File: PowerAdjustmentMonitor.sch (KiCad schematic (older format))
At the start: 19 parts

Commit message: Refactoring and Created key shortcuts
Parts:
- removed R? (x2): R, ~, symbol R
- removed U? (x2): LM324, symbol LM324
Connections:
- net labels removed: V+_CURR_MON, V+_MON, V-_CURR_MON, V-_MON
- wire segments 75 -> 53
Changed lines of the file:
@@
 $Descr A4 11693 8268
 encoding utf-8
-Sheet 9 9
+Sheet 7 9
 Title ""
-Date "9 feb 2014"
+Date "18 feb 2014"
 Rev ""
 Comp ""
@@
 Wire Wire Line
 	3150 1650 3150 1500
-Connection ~ 3150 800
 Connection ~ 3150 1650
 $Comp
@@
 Wire Wire Line
 	4050 1650 4050 1750
-Text HLabel 5700 800  0    60   Output ~ 0
+Text HLabel 5700 800  2    60   Output ~ 0
 V+_ADJ
-Text HLabel 5500 5700 0    60   Output ~ 0
+Text HLabel 5500 5700 2    60   Output ~ 0
 V-_ADJ
-Text HLabel 10100 2300 0    60   Output ~ 0
+Text HLabel 10100 2300 2    60   Output ~ 0
 3V3_MON
-Text HLabel 10100 2550 0    60   Output ~ 0
+Text HLabel 10100 2550 2    60   Output ~ 0
 5V_MON
-Text HLabel 10100 2900 0    60   Output ~ 0
+Text HLabel 10100 2900 2    60   Output ~ 0
 V+_ADJ_MON
-Text HLabel 10100 3200 0    60   Output ~ 0
+Text HLabel 10100 3200 2    60   Output ~ 0
 V-_ADJ_MON
-Text HLabel 10200 4550 0    60   Output ~ 0
-V+_CURR_MON
-Text HLabel 10200 6000 0    60   Output ~ 0
-V-_CURR_MON
 $Comp
 L R R?
@@
 Wire Wire Line
 	8850 2300 10100 2300
-$Comp
-L R R?
-U 1 1 52F6ED35
-P 4050 5700
-F 0 "R?" V 4130 5700 40  0000 C CNN
-F 1 "R" V 4057 5701 40  0000 C CNN
-F 2 "~" V 3980 5700 30  0000 C CNN
-F 3 "~" H 4050 5700 30  0000 C CNN
-	1    4050 5700
-	0    -1   -1   0
-$EndComp
-Wire Wire Line
-	2900 5700 3800 5700
-Wire Wire Line
-	4300 5700 5500 5700
-Wire Wire Line
-	2850 800  3700 800
-Wire Wire Line
-	4200 800  5700 800
-$Comp
-L R R?
-U 1 1 52F6EEF0
-P 3950 800
-F 0 "R?" V 4030 800 40  0000 C CNN
-F 1 "R" V 3957 801 40  0000 C CNN
-F 2 "~" V 3880 800 30  0000 C CNN
-F 3 "~" H 3950 800 30  0000 C CNN
-	1    3950 800
-	0    -1   -1   0
-$EndComp
-Wire Wire Line
-	3600 5700 3600 5500
-Wire Wire Line
-	3600 5500 4150 5500
-Connection ~ 3600 5700
-Text Label 3850 5500 0    60   ~ 0
-V-_MON
-Wire Wire Line
-	3550 800  3550 1150
-Wire Wire Line
-	3550 1150 4250 1150
-Connection ~ 3550 800
-Text Label 3850 1150 0    60   ~ 0
-V+_MON
-$Comp
-L LM324 U?
-U 1 1 52F6FECD
-P 8800 6000
-F 0 "U?" H 8850 6200 60  0000 C CNN
-F 1 "LM324" H 8950 5800 50  0000 C CNN
-F 2 "" H 8800 6000 60  0000 C CNN
-F 3 "" H 8800 6000 60  0000 C CNN
-	1    8800 6000
-	1    0    0    -1
-$EndComp
-$Comp
-L +12V #PWR?
-U 1 1 52F6FEE1
-P 8700 5500
-F 0 "#PWR?" H 8700 5450 20  0001 C CNN
-F 1 "+12V" H 8700 5600 30  0000 C CNN
-F 2 "" H 8700 5500 60  0000 C CNN
-F 3 "" H 8700 5500 60  0000 C CNN
-	1    8700 5500
-	-1   0    0    -1
-$EndComp
-$Comp
-L -12V #PWR?
-U 1 1 52F6FEF0
-P 8700 6600
-F 0 "#PWR?" H 8700 6730 20  0001 C CNN
-F 1 "-12V" H 8700 6700 30  0000 C CNN
-F 2 "" H 8700 6600 60  0000 C CNN
-F 3 "" H 8700 6600 60  0000 C CNN
-	1    8700 6600
-	1    0    0    1
-$EndComp
-Wire Wire Line
-	8700 5500 8700 5600
-Wire Wire Line
-	8700 6400 8700 6600
-$Comp
-L LM324 U?
-U 1 1 52F6FFA1
-P 8800 4550
-F 0 "U?" H 8850 4750 60  0000 C CNN
-F 1 "LM324" H 8950 4350 50  0000 C CNN
-F 2 "" H 8800 4550 60  0000 C CNN
-F 3 "" H 8800 4550 60  0000 C CNN
-	1    8800 4550
-	1    0    0    -1
-$EndComp
-$Comp
-L +12V #PWR?
-U 1 1 52F6FFA7
-P 8700 4050
-F 0 "#PWR?" H 8700 4000 20  0001 C CNN
-F 1 "+12V" H 8700 4150 30  0000 C CNN
-F 2 "" H 8700 4050 60  0000 C CNN
-F 3 "" H 8700 4050 60  0000 C CNN
-	1    8700 4050
-	-1   0    0    -1
-$EndComp
-$Comp
-L -12V #PWR?
-U 1 1 52F6FFAD
-P 8700 5150
-F 0 "#PWR?" H 8700 5280 20  0001 C CNN
-F 1 "-12V" H 8700 5250 30  0000 C CNN
-F 2 "" H 8700 5150 60  0000 C CNN
-F 3 "" H 8700 5150 60  0000 C CNN
-	1    8700 5150
-	1    0    0    1
-$EndComp
-Wire Wire Line
-	8700 4050 8700 4150
-Wire Wire Line
-	8700 4950 8700 5150
-Wire Wire Line
-	9300 4550 10200 4550
-Wire Wire Line
-	9300 6000 10200 6000
-Wire Wire Line
-	8300 4650 8200 4650
-Wire Wire Line
-	8200 4650 8200 5300
-Wire Wire Line
-	8200 5300 9450 5300
-Wire Wire Line
-	9450 5300 9450 4550
-Connection ~ 9450 4550
-Wire Wire Line
-	8300 6100 8150 6100
-Wire Wire Line
-	8150 6100 8150 6800
-Wire Wire Line
-	8150 6800 9450 6800
-Wire Wire Line
-	9450 6800 9450 6000
-Connection ~ 9450 6000
-Wire Wire Line
-	8300 5900 7550 5900
-Wire Wire Line
-	8300 4450 7600 4450
-Text Label 7700 4450 0    60   ~ 0
-V+_MON
-Text Label 7650 5900 0    60   ~ 0
-V-_MON
+Wire Wire Line
+	2900 5700 5500 5700
+Wire Wire Line
+	2850 800  5700 800
 $Comp
 L RVAR R?

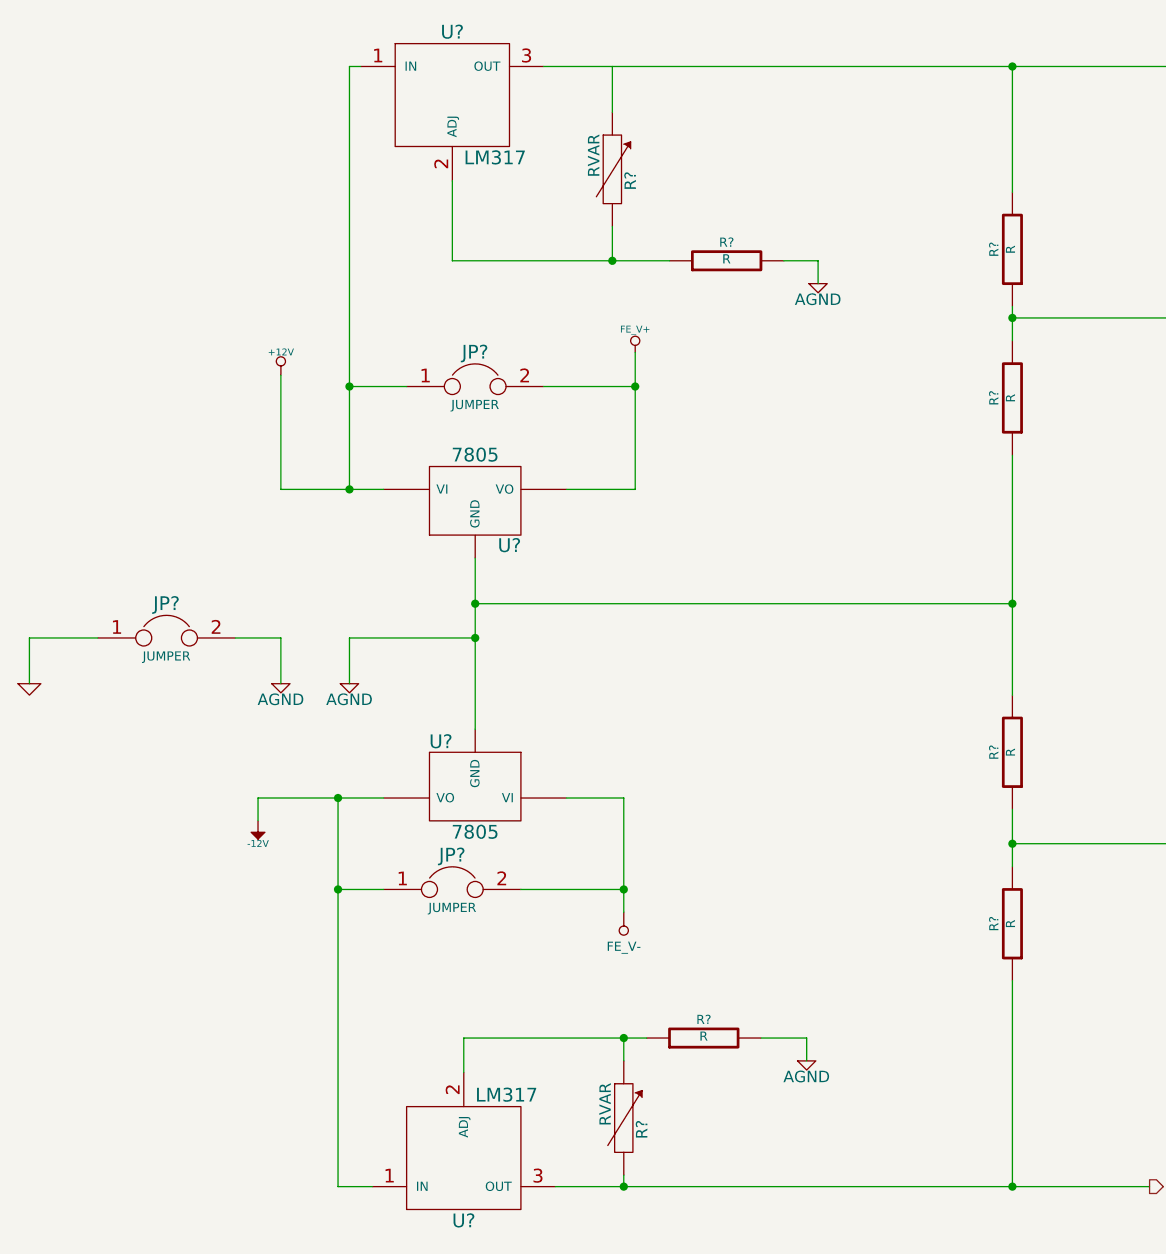
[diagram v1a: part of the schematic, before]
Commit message: Relay module association and placement
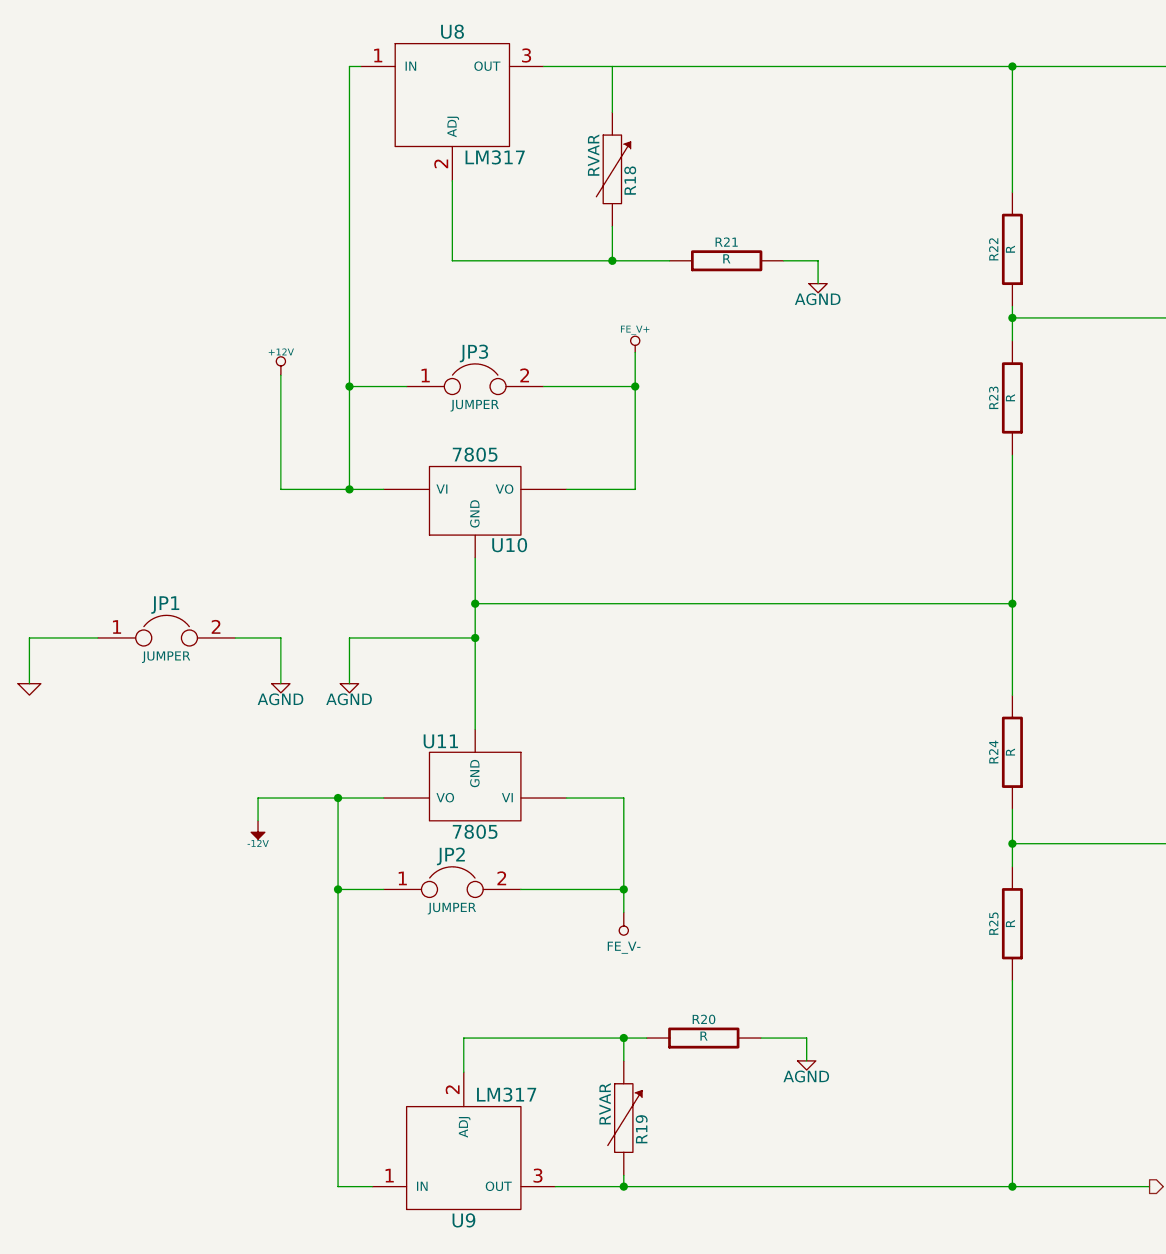
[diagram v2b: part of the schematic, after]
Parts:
- gave numbers to parts that had none: 15
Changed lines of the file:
@@
 Sheet 7 9
 Title ""
-Date "18 feb 2014"
+Date "20 feb 2014"
 Rev ""
 Comp ""
@@
 $EndDescr
 $Comp
-L +5V #PWR?
+L +5V #PWR034
 U 1 1 52F69910
 P 8550 2050
-F 0 "#PWR?" H 8550 2140 20  0001 C CNN
+F 0 "#PWR034" H 8550 2140 20  0001 C CNN
 F 1 "+5V" H 8550 2140 30  0000 C CNN
 F 2 "" H 8550 2050 60  0000 C CNN
@@
 $EndComp
 $Comp
-L +3.3V #PWR?
+L +3.3V #PWR035
 U 1 1 52F69916
 P 8850 2050
-F 0 "#PWR?" H 8850 2010 30  0001 C CNN
+F 0 "#PWR035" H 8850 2010 30  0001 C CNN
 F 1 "+3.3V" H 8850 2160 30  0000 C CNN
 F 2 "" H 8850 2050 60  0000 C CNN
@@
 $EndComp
 $Comp
-L -12V #PWR?
+L -12V #PWR036
 U 1 1 52F699A1
 P 1600 4100
-F 0 "#PWR?" H 1600 4230 20  0001 C CNN
+F 0 "#PWR036" H 1600 4230 20  0001 C CNN
 F 1 "-12V" H 1600 4200 30  0000 C CNN
 F 2 "" H 1600 4100 60  0000 C CNN
@@
 $EndComp
 $Comp
-L +12V #PWR?
+L +12V #PWR037
 U 1 1 52F699A7
 P 1700 2150
-F 0 "#PWR?" H 1700 2100 20  0001 C CNN
+F 0 "#PWR037" H 1700 2100 20  0001 C CNN
 F 1 "+12V" H 1700 2250 30  0000 C CNN
 F 2 "" H 1700 2150 60  0000 C CNN
@@
 	1700 2150 1700 2650
 $Comp
-L LM317 U?
+L LM317 U8
 U 1 1 52F69E71
 P 2450 950
-F 0 "U?" H 2450 1250 60  0000 C CNN
+F 0 "U8" H 2450 1250 60  0000 C CNN
 F 1 "LM317" H 2500 700 60  0000 L CNN
 F 2 "~" H 2450 950 60  0000 C CNN
@@
 $EndComp
 $Comp
-L LM317 U?
+L LM317 U9
 U 1 1 52F69E80
 P 2500 5550
-F 0 "U?" H 2500 5850 60  0000 C CNN
+F 0 "U9" H 2500 5850 60  0000 C CNN
 F 1 "LM317" H 2550 5300 60  0000 L CNN
 F 2 "~" H 2500 5550 60  0000 C CNN
@@
 	1600 4000 2150 4000
 $Comp
-L JUMPER JP?
+L JUMPER JP2
 U 1 1 52F69EAE
 P 2450 4400
-F 0 "JP?" H 2450 4550 60  0000 C CNN
+F 0 "JP2" H 2450 4550 60  0000 C CNN
 F 1 "JUMPER" H 2450 4320 40  0000 C CNN
 F 2 "~" H 2450 4400 60  0000 C CNN
@@
 	3200 4000 2950 4000
 $Comp
-L JUMPER JP?
+L JUMPER JP3
 U 1 1 52F69ECB
 P 2550 2200
-F 0 "JP?" H 2550 2350 60  0000 C CNN
+F 0 "JP3" H 2550 2350 60  0000 C CNN
 F 1 "JUMPER" H 2550 2120 40  0000 C CNN
 F 2 "~" H 2550 2200 60  0000 C CNN
@@
 	3250 2200 2850 2200
 $Comp
-L GND #PWR?
+L GND #PWR038
 U 1 1 52F69EEF
 P 600 3500
-F 0 "#PWR?" H 600 3500 30  0001 C CNN
+F 0 "#PWR038" H 600 3500 30  0001 C CNN
 F 1 "GND" H 600 3430 30  0001 C CNN
 F 2 "" H 600 3500 60  0000 C CNN
@@
 $EndComp
 $Comp
-L AGND #PWR?
+L AGND #PWR039
 U 1 1 52F69F10
 P 1700 3500
-F 0 "#PWR?" H 1700 3500 40  0001 C CNN
+F 0 "#PWR039" H 1700 3500 40  0001 C CNN
 F 1 "AGND" H 1700 3430 50  0000 C CNN
 F 2 "" H 1700 3500 60  0000 C CNN
@@
 $EndComp
 $Comp
-L JUMPER JP?
+L JUMPER JP1
 U 1 1 52F69F27
 P 1200 3300
-F 0 "JP?" H 1200 3450 60  0000 C CNN
+F 0 "JP1" H 1200 3450 60  0000 C CNN
 F 1 "JUMPER" H 1200 3220 40  0000 C CNN
 F 2 "~" H 1200 3300 60  0000 C CNN
@@
 	1700 3300 1700 3500
 $Comp
-L AGND #PWR?
+L AGND #PWR040
 U 1 1 52F69F75
 P 2000 3500
-F 0 "#PWR?" H 2000 3500 40  0001 C CNN
+F 0 "#PWR040" H 2000 3500 40  0001 C CNN
 F 1 "AGND" H 2000 3430 50  0000 C CNN
 F 2 "" H 2000 3500 60  0000 C CNN
@@
 	2000 3500 2000 3300
 $Comp
-L FE_V+ #PWR?
+L FE_V+ #PWR041
 U 1 1 52F6E408
 P 3250 2050
-F 0 "#PWR?" H 3250 2150 30  0001 C CNN
+F 0 "#PWR041" H 3250 2150 30  0001 C CNN
 F 1 "FE_V+" H 3250 2150 30  0000 C CNN
 F 2 "" H 3250 2050 60  0000 C CNN
@@
 Connection ~ 3250 2200
 $Comp
-L FE_V- #PWR?
+L FE_V- #PWR41
 U 1 1 52F6E430
 P 3200 4500
-F 0 "#PWR?" H 3200 4700 40  0001 C CNN
+F 0 "#PWR41" H 3200 4700 40  0001 C CNN
 F 1 "FE_V-" H 3200 4650 40  0000 C CNN
 F 2 "" H 3200 4500 60  0000 C CNN
@@
 Connection ~ 3200 4400
 $Comp
-L 7805 U?
+L 7805 U10
 U 1 1 52F6E65F
 P 2550 2700
-F 0 "U?" H 2700 2504 60  0000 C CNN
+F 0 "U10" H 2700 2504 60  0000 C CNN
 F 1 "7805" H 2550 2900 60  0000 C CNN
 F 2 "~" H 2550 2700 60  0000 C CNN
@@
 $EndComp
 $Comp
-L 7805 U?
+L 7805 U11
 U 1 1 52F6E66C
 P 2550 3950
-F 0 "U?" H 2700 3754 60  0000 C CNN
+F 0 "U11" H 2700 3754 60  0000 C CNN
 F 1 "7805" H 2550 4150 60  0000 C CNN
 F 2 "~" H 2550 3950 60  0000 C CNN
@@
 Connection ~ 2000 2200
 $Comp
-L R R?
+L R R20
 U 1 1 52F6E74A
 P 3550 5050
-F 0 "R?" V 3630 5050 40  0000 C CNN
+F 0 "R20" V 3630 5050 40  0000 C CNN
 F 1 "R" V 3557 5051 40  0000 C CNN
 F 2 "~" V 3480 5050 30  0000 C CNN
@@
 Connection ~ 3200 5050
 $Comp
-L AGND #PWR?
+L AGND #PWR042
 U 1 1 52F6E7E7
 P 4000 5150
-F 0 "#PWR?" H 4000 5150 40  0001 C CNN
+F 0 "#PWR042" H 4000 5150 40  0001 C CNN
 F 1 "AGND" H 4000 5080 50  0000 C CNN
 F 2 "" H 4000 5150 60  0000 C CNN
@@
 Connection ~ 3200 5700
 $Comp
-L R R?
+L R R21
 U 1 1 52F6E841
 P 3650 1650
-F 0 "R?" V 3730 1650 40  0000 C CNN
+F 0 "R21" V 3730 1650 40  0000 C CNN
 F 1 "R" V 3657 1651 40  0000 C CNN
 F 2 "~" V 3580 1650 30  0000 C CNN
@@
 Connection ~ 3150 1650
 $Comp
-L AGND #PWR?
+L AGND #PWR043
 U 1 1 52F6E999
 P 4050 1750
-F 0 "#PWR?" H 4050 1750 40  0001 C CNN
+F 0 "#PWR043" H 4050 1750 40  0001 C CNN
 F 1 "AGND" H 4050 1680 50  0000 C CNN
 F 2 "" H 4050 1750 60  0000 C CNN
@@
 V-_ADJ_MON
 $Comp
-L R R?
+L R R22
 U 1 1 52F6EA99
 P 4900 1600
-F 0 "R?" V 4980 1600 40  0000 C CNN
+F 0 "R22" V 4980 1600 40  0000 C CNN
 F 1 "R" V 4907 1601 40  0000 C CNN
 F 2 "~" V 4830 1600 30  0000 C CNN
@@
 $EndComp
 $Comp
-L R R?
+L R R23
 U 1 1 52F6EA9F
 P 4900 2250
-F 0 "R?" V 4980 2250 40  0000 C CNN
+F 0 "R23" V 4980 2250 40  0000 C CNN
 F 1 "R" V 4907 2251 40  0000 C CNN
 F 2 "~" V 4830 2250 30  0000 C CNN
@@
 Connection ~ 2550 3150
 $Comp
-L R R?
+L R R24
 U 1 1 52F6EB3D
 P 4900 3800
-F 0 "R?" V 4980 3800 40  0000 C CNN
+F 0 "R24" V 4980 3800 40  0000 C CNN
 F 1 "R" V 4907 3801 40  0000 C CNN
 F 2 "~" V 4830 3800 30  0000 C CNN
@@
 $EndComp
 $Comp
-L R R?
+L R R25
 U 1 1 52F6EB43
 P 4900 4550
-F 0 "R?" V 4980 4550 40  0000 C CNN
+F 0 "R25" V 4980 4550 40  0000 C CNN
 F 1 "R" V 4907 4551 40  0000 C CNN
 F 2 "~" V 4830 4550 30  0000 C CNN
@@
 	2850 800  5700 800
 $Comp
-L RVAR R?
+L RVAR R19
 U 1 1 52F701D6
 P 3200 5400
-F 0 "R?" V 3280 5350 50  0000 C CNN
+F 0 "R19" V 3280 5350 50  0000 C CNN
 F 1 "RVAR" V 3120 5460 50  0000 C CNN
 F 2 "~" H 3200 5400 60  0000 C CNN
@@
 $EndComp
 $Comp
-L RVAR R?
+L RVAR R18
 U 1 1 52F7024E
 P 3150 1250
-F 0 "R?" V 3230 1200 50  0000 C CNN
+F 0 "R18" V 3230 1200 50  0000 C CNN
 F 1 "RVAR" V 3070 1310 50  0000 C CNN
 F 2 "~" H 3150 1250 60  0000 C CNN

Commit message: Power Adjustment: assc/placement
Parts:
- removed JP2, JP3: JUMPER, ~, symbol JUMPER
- removed R19: RVAR, ~, symbol RVAR
- removed U10, U11: 7805, ~, symbol 7805
- removed U9: LM317, ~, symbol LM317
- added C14, C15, C16, C17, C18, C19, C20, C21, C22, C23, C24, C25: C, ~, symbol C
- added D10, D11, D12, D3, D6, D7, D8, D9: MMBD914-7-F, ~, symbol DIODE
- added R19, R52, R53: R, ~, symbol R
- added R54: 715, ~, symbol R
- added R55: 5K, ~, symbol RVAR
- added U10, U9: LM337T, TO-220, symbol LM337T
- added U7: LM317, ~, symbol LM317
- R18: value RVAR -> 5K
- R21: value R -> 715
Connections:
- net +12V: now also C14.1, C16.1, D6.2 (K), D8.2 (K), U7.1 (IN)
- net -12V: now also C15.2, C19.2, D10.1 (A), D3.1 (A), U10.2 (IN), U9.2 (IN)
- net AGND: now also R18.2, R20.1, C14.2, C15.1, C16.2, C17.2, C18.1, C19.1, C20.2, C21.2, C22.1, C23.1, C24.2, C25.1, R52.2, R55.2; no longer R20.2, R21.2
- net FE_V+: now also C20.1, D6.1 (A), D7.2 (K), R19.2, U7.3 (OUT)
- net FE_V-: now also C22.2, D3.2 (K), D9.1 (A), R53.1, U9.3 (OUT)
- net V+_ADJ: now also R21.2, C24.1, D11.2 (K), D8.1 (A)
- net V-_ADJ: now also C25.2, D10.2 (K), D12.1 (A), R54.1, U10.3 (OUT)
- net at R21.1, U8.2 (ADJ): now also R18.1, C21.1, D11.1 (A); no longer R18.2
- new net: C17.1, D7.1 (A), R19.1, R20.2, U7.2 (ADJ)
- new net: C18.2, D9.2 (K), R52.1, R53.2, U9.1 (ADJ)
- new net: C23.2, D12.2 (K), R54.2, R55.1, U10.1 (ADJ)
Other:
- note added: "-1.5 to -10V OUTPUT"
- note added: "-10V OUTPUT"
- note added: "1.5 to 10V OUTPUT"
- note added: "10V OUTPUT"
- moved on the sheet: JP1, R18, R21, R22, R23, R24, R25, U8
